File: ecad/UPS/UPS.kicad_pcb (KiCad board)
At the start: 4 copper layers, 177.8 x 139.7 mm, 160 parts, among them J1 Barrel_Jack, J2 Conn_01x02_Socket, J3 USB_C_Receptacle_USB2.0_16P, J4 PROG, Q1 CSD18540Q5B, Q2 Q_PMOS_DGS, Q3 IRLR7843TRPBF, Q4 Q_PMOS_DGS, Q5 CSD18540Q5B, Q6 CSD18540Q5B, Q7 CSD18540Q5B, SW3 SW_DPDT_x2, U1 BQ25730RSNR, U2 MPQ5031GRE-0001-AEC1-P, U3 L78L05_SOT89, U4 STM32L152RCT6, U5 AP2112K-3.3TRG1, U6 BOOT0, U7 NRST

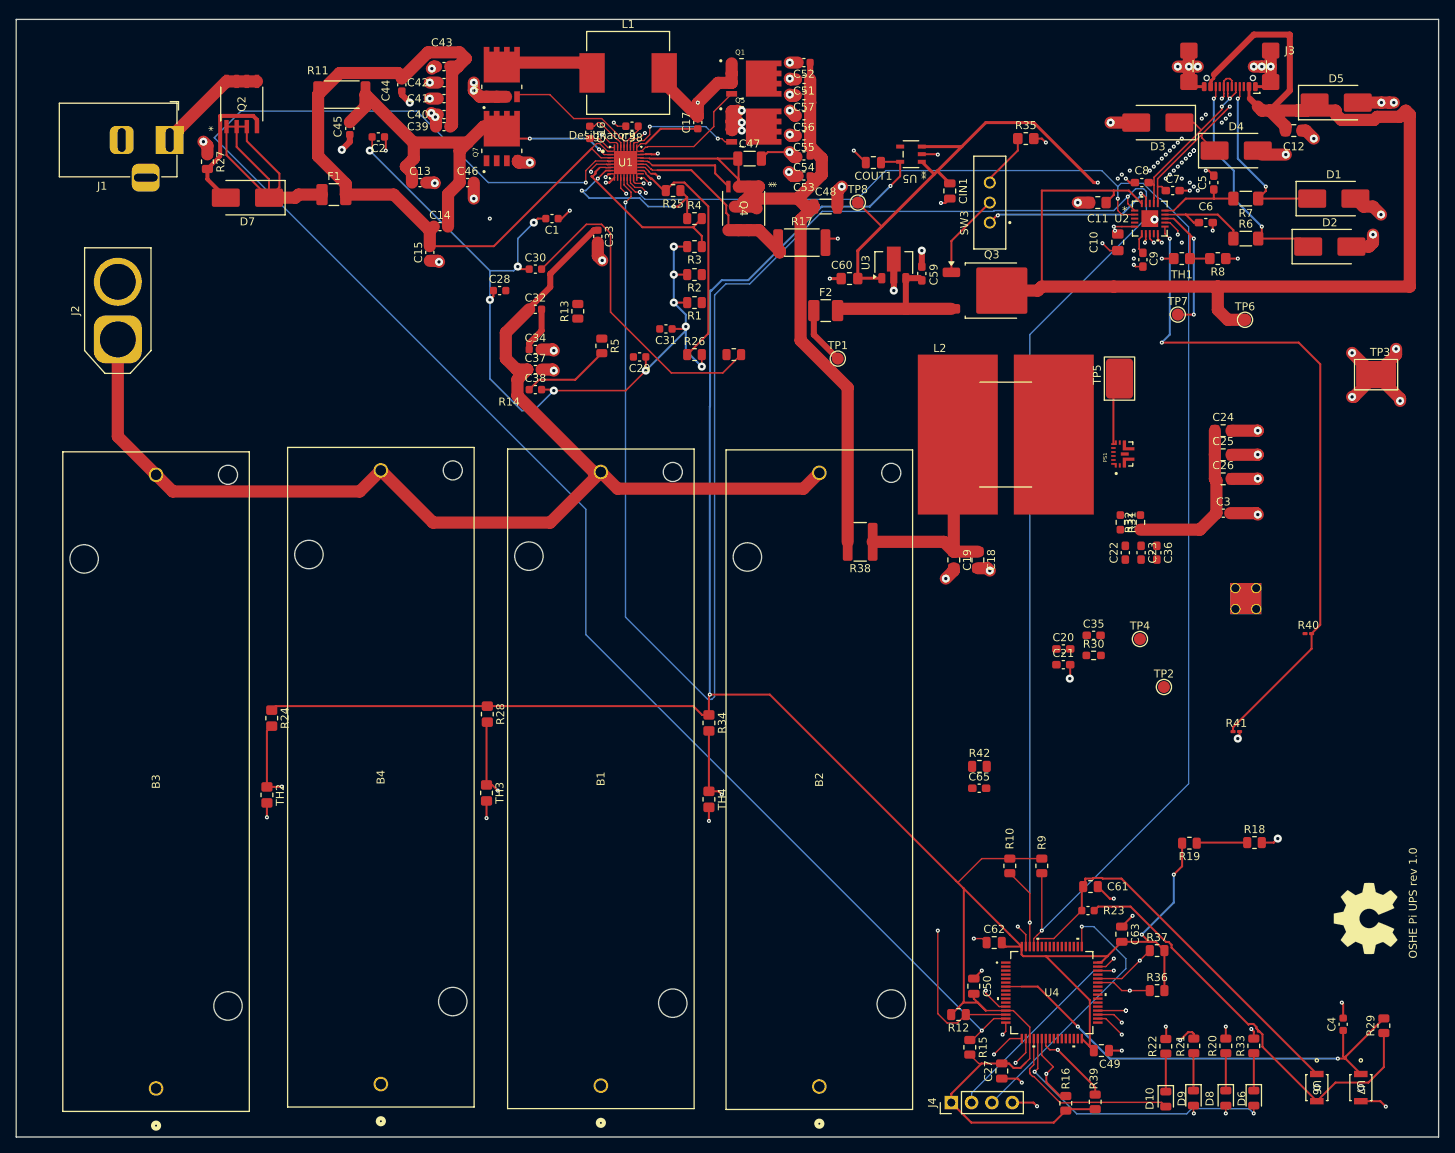
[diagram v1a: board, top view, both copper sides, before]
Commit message: Moved batteries to back, experimenting with different layouts
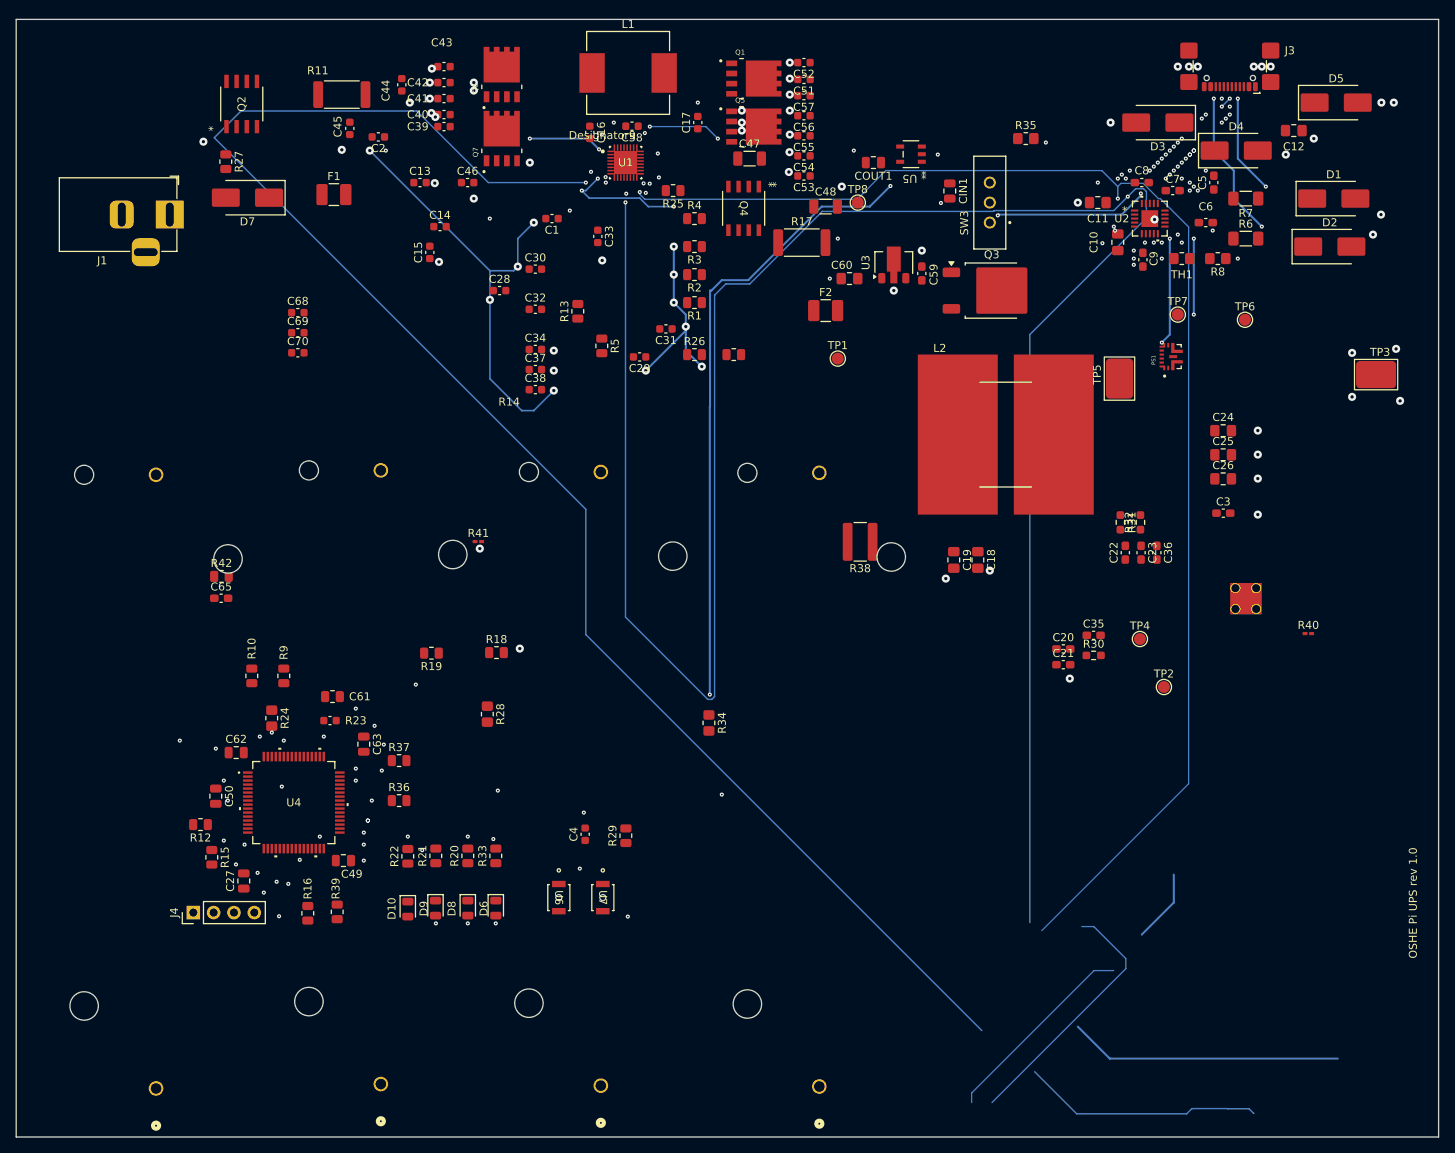
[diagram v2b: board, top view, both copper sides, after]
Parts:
- removed J2: Conn_01x02_Socket, Connector_AMASS:AMASS_XT60-F_1x02_P7.20mm_Vertical
- removed REF**: OSHW-Symbol_8.9x8mm_SilkScreen, Symbol:OSHW-Symbol_8.9x8mm_SilkScreen
- removed TH2, TH3, TH4: B57471V2104J062, Resistor_SMD:R_0805_2012Metric_Pad1.20x1.40mm_HandSolder
- added C68: 100 nF, Capacitor_SMD:C_0603_1608Metric, F.Cu at (86.0, 74.8)
- added C69: 100 nF, Capacitor_SMD:C_0603_1608Metric, F.Cu at (86.0, 77.3)
- added C70: 100 nF, Capacitor_SMD:C_0603_1608Metric, F.Cu at (86.0, 79.8)
- B1, B2, B3, B4: moved to B.Cu
- moved C65 97.7 mm to (76.4, 110.5)
- moved C61 97.7 mm to (90.0, 125.8)
- moved C62 97.7 mm to (78.3, 129.8)
- moved D9 97.7 mm to (103.2, 149.2)
- moved R12 97.7 mm to (73.8, 138.8)
- moved R18 97.7 mm to (110.8, 117.3)
- moved R23 97.7 mm to (90.3, 122.8)
- moved R39 97.7 mm to (90.9, 149.7)
- moved R42 97.7 mm to (76.5, 107.7)
- moved U6 97.7 mm to (118.6, 147.9)
- moved U7 97.7 mm to (124.1, 147.9)
- moved C27 97.7 mm to (79.2, 145.8)
- moved C4 97.7 mm to (121.9, 140.0)
- moved C50 97.7 mm to (75.7, 135.2)
- moved C63 97.7 mm to (94.2, 128.7)
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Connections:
- net /controller/vbat_sense renamed /controller/VBAT_SENSE
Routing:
- net +3.3V: track 334.6 -> 87.6 mm
- net PGND: track 201.7 -> 1.01 mm, vias 130 -> 144
- net /Output/VBUS_out: track 159.8 -> 0.00 mm
- net /Charger/VBAT_SENSE: track 183.4 -> 25.5 mm
- net /Charger/bat_th2: track 155.2 -> 0.00 mm, vias 2 -> 0
- net NRST: track 59.6 -> 176.4 mm, vias 2 -> 3
- net PMOS_OUT_GATE: track 107.7 -> 0.00 mm
- net /Charger/Charger_VBUS_IN: track 91.8 -> 0.00 mm
- net Net-(U2-GPIO2): track 86.5 -> 0.00 mm, vias 2 -> 0
- net +5V: track 93.0 -> 27.8 mm
- net 3.3V: track 53.9 -> 0.00 mm
- net Net-(U4B-BOOT0): track 51.2 -> 0.00 mm
- net Net-(U1-ACN): track 56.3 -> 9.21 mm
- net PMOS_IN_GATE: track 42.1 -> 0.00 mm
- net Net-(C30-Pad2): track 41.7 -> 0.00 mm
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
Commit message: Got VBAT_SENSE labels fixed, wasn't a sheet pin for some reason
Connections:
- C65 pad 1: /controller/VBAT_SENSE -> /Charger/VBAT_SENSE
- R40 pad 1: /Output/vbat_sense -> /Charger/VBAT_SENSE
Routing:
- net /Charger/VBAT_SENSE: track 25.5 -> 0.00 mm, vias 2 -> 0
- net (no net): track 1.00 -> 26.5 mm, vias 1 -> 3

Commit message: Couple missing footprints added, Need to look into USB route, make sure voltage regulator is fine as is
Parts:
- added C64: 1nF, Capacitor_SMD:C_0603_1608Metric_Pad1.08x0.95mm_HandSolder, F.Cu at (209.3, 116.8)
- added J2: Conn_01x02_Pin, Connector_JST:JST_XH_B2B-XH-A_1x02_P2.50mm_Vertical, F.Cu at (190.0, 143.4)
- added J5: Conn_01x02_Pin, Connector_JST:JST_XH_B2B-XH-A_1x02_P2.50mm_Vertical, F.Cu at (190.0, 151.2)
- added J6: Conn_01x02_Pin, Connector_JST:JST_XH_B2B-XH-A_1x02_P2.50mm_Vertical, F.Cu at (190.0, 167.5)
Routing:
- net GNDA: track 79.5 -> 88.6 mm
- net +3.3V: track 87.6 -> 78.5 mm

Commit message: Board cleanup from during meeting
Removed old traces on layers 3,4
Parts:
- moved J5 30.9 mm to (162.0, 138.0)
- moved J2 17.6 mm to (177.5, 131.0)
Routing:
- net /Output/SDA: track 274.6 -> 0.00 mm, vias 2 -> 0
- net /Charger/chrg_ok: track 202.9 -> 0.00 mm
- net NRST: track 176.4 -> 0.00 mm
- net /Charger/bat_th1: track 175.0 -> 0.00 mm, vias 2 -> 4
- net /Output/SCL: track 170.9 -> 0.00 mm
- net /Charger/OTG/VAP: track 140.9 -> 0.00 mm
- net /Charger/cmp_out: track 130.0 -> 0.00 mm
- net /Charger/PROCHOT_N: track 108.4 -> 0.00 mm
- net /Charger/bat_th3: track 108.1 -> 0.00 mm
- net /Output/vsel2: track 104.3 -> 0.00 mm
- net GNDA: track 88.6 -> 0.00 mm
- net +3.3V: track 78.5 -> 0.00 mm
- net PA14_SWCLK: track 32.1 -> 0.00 mm
- net Net-(D8-A): track 32.0 -> 0.00 mm
- net Net-(D6-A): track 30.1 -> 0.00 mm
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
